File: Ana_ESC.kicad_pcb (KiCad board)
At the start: 4 copper layers, 90 x 90 mm, 106 parts, among them IC3 TCAN330DCNT, J1 BM04B-GHS-TBT_LF__SN__N_, J2 Conn_01x04_Pin, J3 USB_C_Receptacle_USB2.0_16P, J4 BM04B-GHS-TBT_LF__SN__N_, J5 Conn_01x02_Socket, Q10 STL90N6F7, Q11 STL90N6F7, Q12 STL90N6F7, Q7 STL90N6F7, Q8 STL90N6F7, Q9 STL90N6F7, SW1 SW_SPDT, SW2 SW_SPDT, U1 DRV8323RSRGZR, U2 STM32G431CBU6, U3 ME6211C33M5, Y1 ECS-80-20-5PX-TR

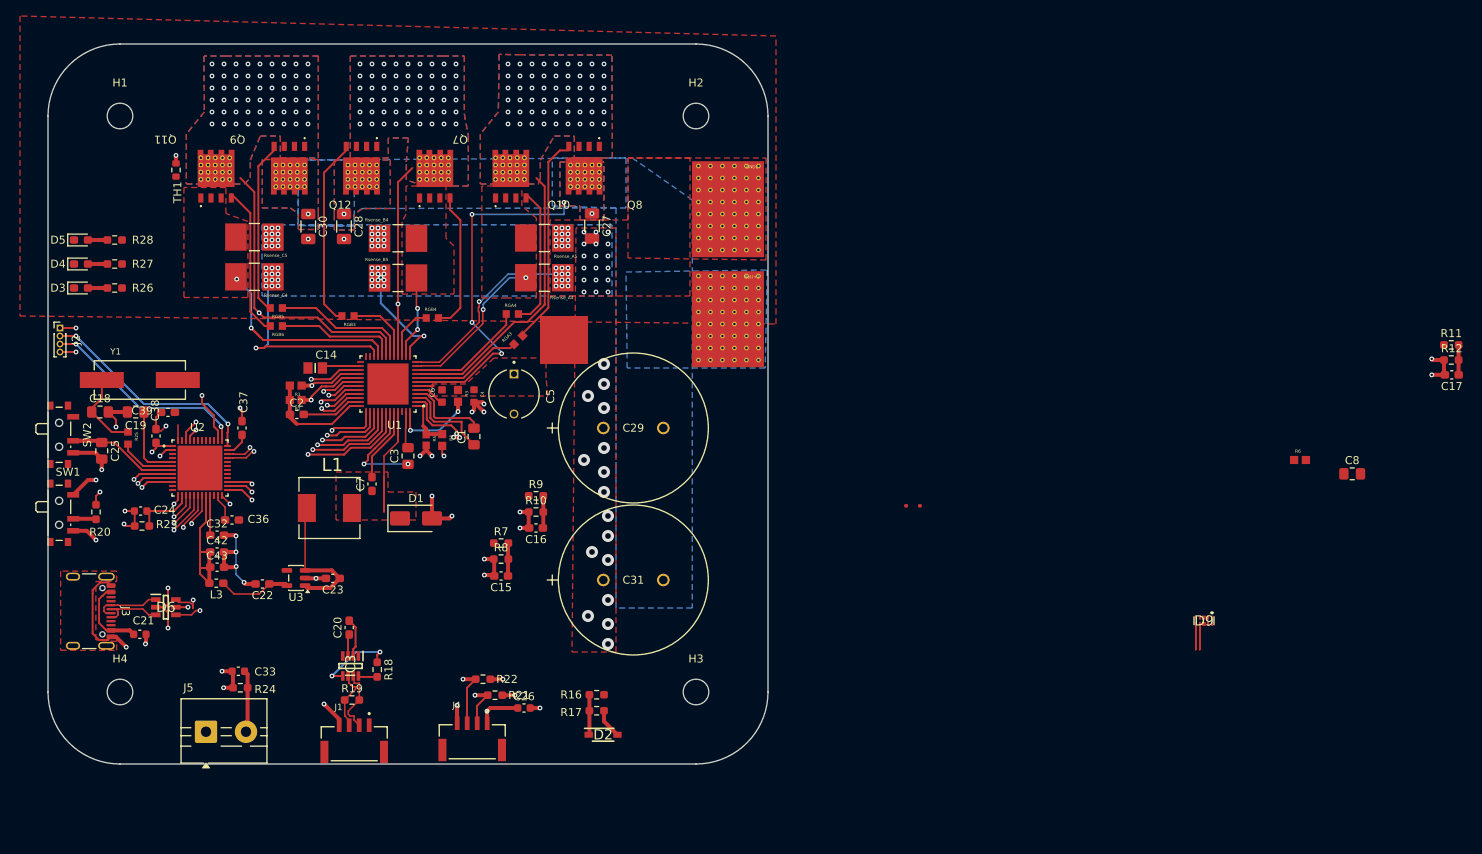
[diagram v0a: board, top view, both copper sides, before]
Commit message: Some pcb design and schematics editings about PGND_DRV
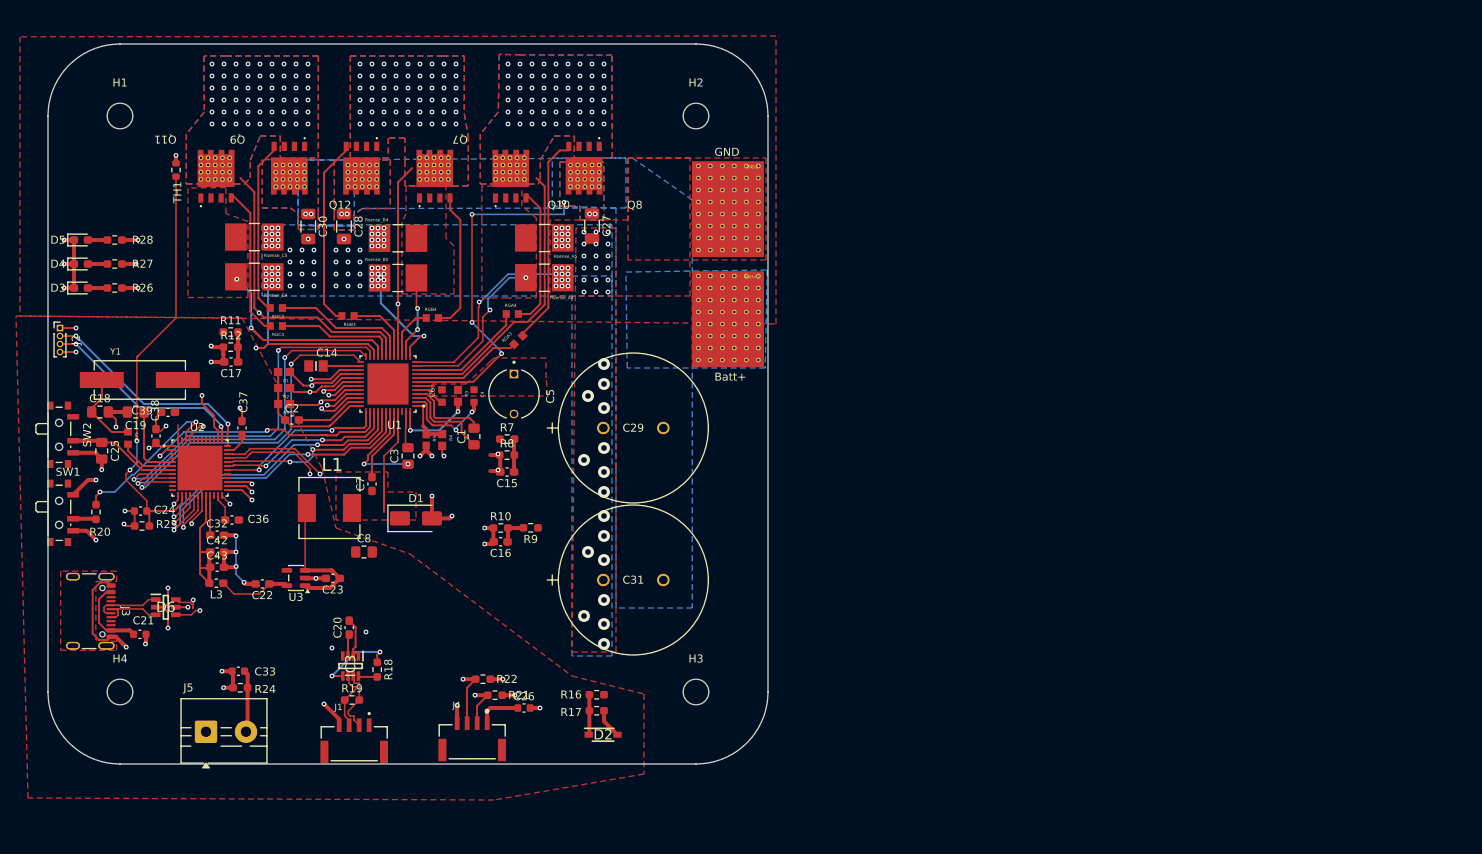
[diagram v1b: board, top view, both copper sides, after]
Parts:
- removed D9: ESD7104MUTAG, LIB_ESD7104MUTAG:ESD8104MUTAG
- removed NT1: NetTie_4, NetTie:NetTie-4_SMD_Pad2.0mm
- moved C17 152.6 mm to (71.4, 91.2)
- moved R11 152.6 mm to (71.3, 87.5)
- moved R12 152.6 mm to (71.3, 89.4)
- moved R6 127.2 mm to (78.0, 96.5), turned to 180 degrees
- moved C8 123.9 mm to (88.0, 115.0)
- moved C15 13.0 mm to (105.9, 105.0)
- moved R7 13.0 mm to (105.9, 100.9)
- moved R8 13.0 mm to (105.9, 102.9)
- moved R10 4.84 mm to (105.1, 112.0)
- moved C16 4.74 mm to (105.1, 113.7)
- moved R9 4.05 mm to (108.8, 112.0), turned to 180 degrees
- moved R1 2.24 mm to (78.0, 92.5)
- moved R2 2.09 mm to (78.0, 94.5)
- moved C2 0.93 mm to (79.0, 98.5)
- moved C14 0.27 mm to (82.0, 91.8)
- renumbered RGB5 to RGC3, RGB6 to RGC4
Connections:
- C27 pad 2: PGND -> PGND_DRV
- C28 pad 2: GND -> PGND_DRV
- C29 pad 1: GND -> PGND_DRV
- C30 pad 2: GND -> PGND_DRV
- C31 pad 1: GND -> PGND_DRV
- C4 pad 2: /Gate_Driver/PGND -> PGND_DRV
- C5 pad N: /Gate_Driver/PGND -> PGND_DRV
- GND1 pad 1: GND -> PGND_DRV
- Rsense_A4 pad 1: PGND -> PGND_DRV
- Rsense_A5 pad 1: PGND -> PGND_DRV
- Rsense_B4 pad 1: GND -> PGND_DRV
- Rsense_B5 pad 1: GND -> PGND_DRV
- Rsense_C4 pad 1: GND -> PGND_DRV
- Rsense_C5 pad 1: GND -> PGND_DRV
- U1 pad 12: PGND -> PGND_DRV
- U1 pad 13: GND -> PGND_DRV
- U1 pad 22: GND -> PGND_DRV
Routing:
- net PGND_DRV: track 0.00 -> 67.3 mm, vias 0 -> 136
- net /MCU/NTC_FET: track 7.89 -> 53.4 mm, vias 0 -> 2
- net /Gate_Driver/SOC: track 5.10 -> 48.0 mm, vias 1 -> 2
- net /Gate_Driver/SOB: track 4.60 -> 45.6 mm, vias 1 -> 2
- net /Gate_Driver/SOA: track 4.10 -> 43.4 mm, vias 1 -> 2
- net GND: track 147.6 -> 115.6 mm, vias 102 -> 35
- net PGND: track 24.9 -> 0.00 mm, vias 42 -> 0
- net /Gate_Driver/INLB: track 16.0 -> 39.6 mm
- net /Gate_Driver/INLA: track 9.62 -> 32.2 mm
- net /Gate_Driver/INLC: track 18.4 -> 39.1 mm
- net /MCU/BOOT0: track 4.63 -> 20.3 mm
- net /Gate_Driver/INHA: track 6.29 -> 21.7 mm, vias 1 -> 2
- net /Gate_Driver/INHB: track 9.17 -> 22.5 mm, vias 1 -> 2
- net /Gate_Driver/INHC: track 12.1 -> 24.0 mm, vias 1 -> 2
- net /MCU/USB_DP: track 9.79 -> 16.4 mm
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- added copper zone on B.Cu, net PGND_DRV
- added copper zone on F.Cu, net PGND_DRV
- removed copper zone on B.Cu, net GND
- removed copper zone on F.Cu, net PGND
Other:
- board text added: "Batt+"
- board text added: "GND"

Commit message: all routed pcb
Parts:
- moved D3 61.9 mm to (98.3, 123.8), turned to 180 degrees
- moved D4 61.9 mm to (98.3, 120.8), turned to 180 degrees
- moved D5 61.9 mm to (98.3, 117.8), turned to 180 degrees
- moved R26 56.0 mm to (94.1, 123.8), turned to 180 degrees
- moved R27 56.0 mm to (94.1, 120.8), turned to 180 degrees
- moved R28 56.0 mm to (94.1, 117.8), turned to 180 degrees
- moved C16 28.7 mm to (97.8, 86.0)
- moved R10 25.3 mm to (97.8, 87.8)
- moved R9 25.1 mm to (97.8, 89.5), turned to 0 degrees
- moved J3 23.7 mm to (70.7, 137.9), turned to 0 degrees
- moved R11 23.5 mm to (76.0, 110.5), turned to 180 degrees
- moved C17 23.5 mm to (76.0, 114.2), turned to 0 degrees
- moved R12 23.4 mm to (76.0, 112.4), turned to 180 degrees
- moved J5 22.8 mm to (53.0, 120.5), turned to -90 degrees
- moved R24 15.8 mm to (58.5, 124.8), turned to 90 degrees
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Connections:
- C14 pad 1: /Gate_Driver/DGND -> GND
- C2 pad 2: /Gate_Driver/AGND -> GND
- C3 pad 1: /Gate_Driver/BGND -> GND
- J4 pad 3: /MCU/I2C1_SCL -> /MCU/I2C1_SDA
- R22 pad 2: /MCU/I2C1_SCL -> /MCU/I2C1_SDA
- U1 pad 2: /Gate_Driver/PGND -> GND
- U1 pad 27: /Gate_Driver/DGND -> GND
- U1 pad 35: /Gate_Driver/AGND -> GND
- U1 pad 43: /Gate_Driver/BGND -> GND
- U2 pad 45: /MCU/I2C1_SCL -> /MCU/I2C1_SDA
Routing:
- net /MCU/UART_P: track 0.00 -> 85.0 mm, vias 0 -> 2
- net GND: track 115.6 -> 198.1 mm, vias 35 -> 39
- net /MCU/UART_N: track 0.00 -> 78.8 mm, vias 0 -> 2
- net /MCU/I2C1_SDA: track 0.00 -> 76.0 mm, vias 0 -> 2
- net /MCU/VBus: track 9.21 -> 73.9 mm, vias 1 -> 0
- net +3.3V: track 44.4 -> 102.3 mm, vias 7 -> 15
- net MCU_PWR: track 30.2 -> 85.9 mm, vias 2 -> 4
- net /MCU/I2C1_SCL: track 22.8 -> 74.5 mm, vias 4 -> 2
- net VM: track 51.3 -> 90.2 mm
- net /Gate_Driver/SHC: track 37.3 -> 72.1 mm, vias 55 -> 57
- net Net-(U2-PB12): track 5.58 -> 30.7 mm
- net Net-(U2-PB13): track 5.13 -> 30.1 mm
- net /MCU/USB_DP: track 16.4 -> 41.1 mm
- net /MCU/USB_DN: track 16.0 -> 40.0 mm
- net Net-(U2-PB14): track 5.17 -> 28.5 mm
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- added copper zone on In1.Cu, net +3.3V

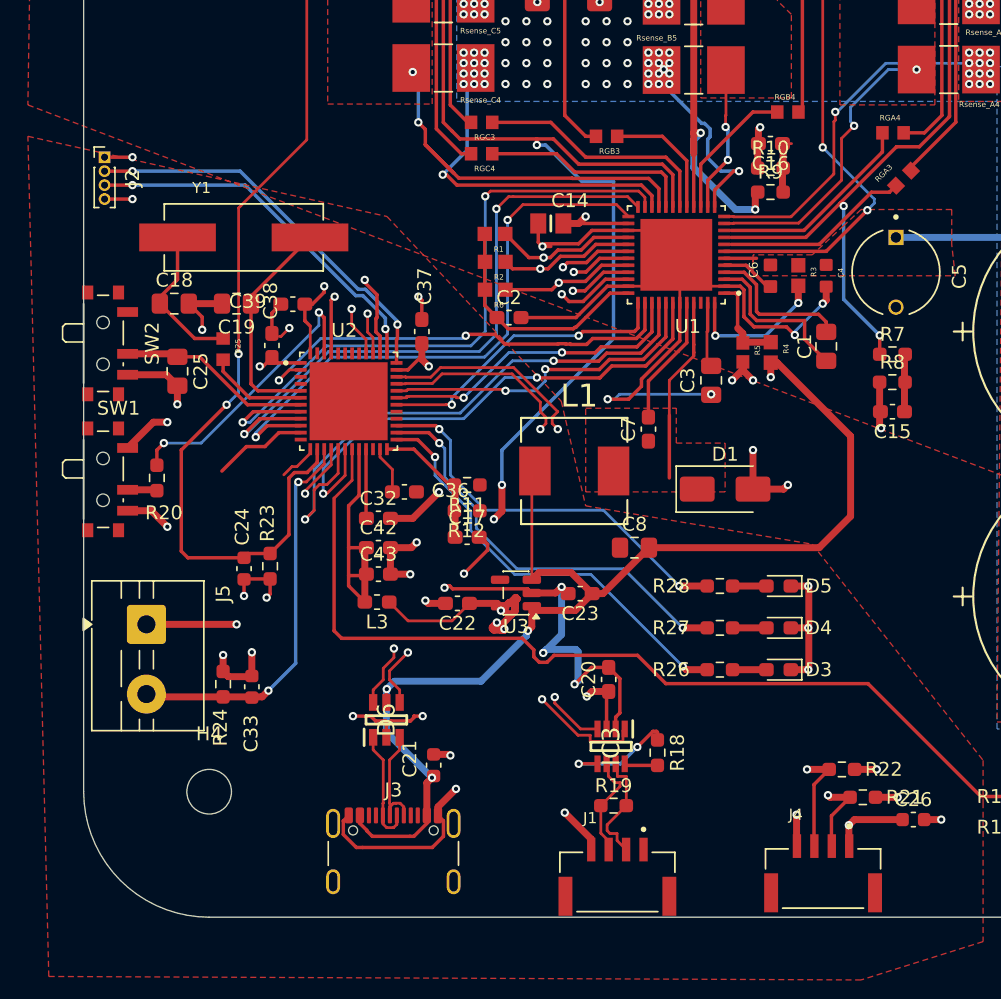
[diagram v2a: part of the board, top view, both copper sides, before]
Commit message: fixing design errors
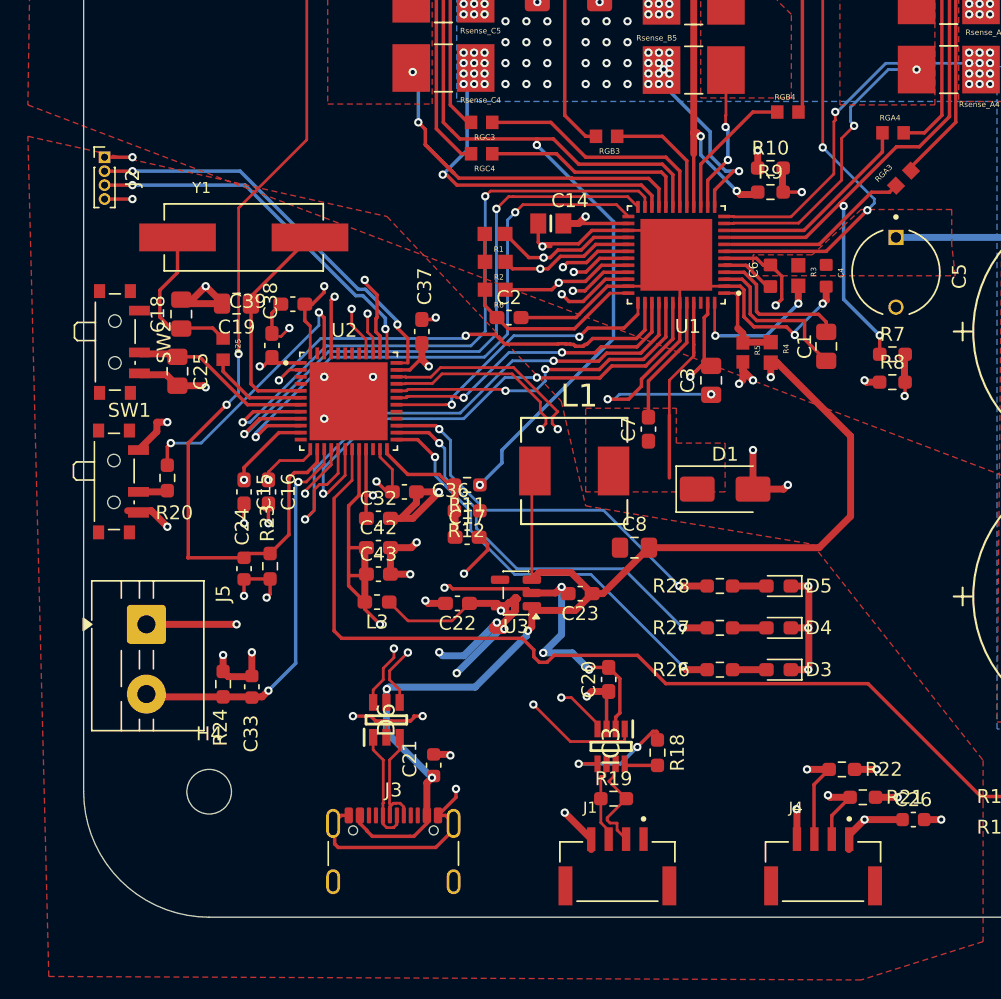
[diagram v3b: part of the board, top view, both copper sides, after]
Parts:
- moved C15 46.9 mm to (60.0, 111.0), turned to -90 degrees
- moved C16 43.8 mm to (61.8, 111.0), turned to -90 degrees
- moved C18 0.90 mm to (55.5, 98.2), turned to 90 degrees
- moved SW2 0.86 mm to (51.1, 100.2)
- moved SW1 0.79 mm to (51.0, 110.2)
- moved J1 0.75 mm to (86.8, 139.2)
- moved R20 0.75 mm to (54.5, 110.0)
- moved J4 0.50 mm to (101.5, 139.2)
- moved R19 0.50 mm to (86.5, 133.0)
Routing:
- net /Gate_Driver/SENS1: track 11.2 -> 92.4 mm, vias 0 -> 2
- net /Gate_Driver/SENS2: track 7.11 -> 61.4 mm, vias 0 -> 2
- net +3.3V: track 102.3 -> 123.5 mm, vias 15 -> 18
- net GND: track 198.1 -> 217.2 mm, vias 39 -> 44
- net VM: track 90.2 -> 106.6 mm, vias 10 -> 12
- net +3.3VA: track 23.2 -> 35.3 mm, vias 0 -> 2
- net /Gate_Driver/SHC: track 72.1 -> 68.4 mm, vias 57 -> 56
- net /Gate_Driver/SHB: track 34.5 -> 31.6 mm
- net /MCU/SWDIO: track 28.5 -> 29.6 mm
- net /MCU/UART_N: track 78.8 -> 79.9 mm
- net /MCU/RST: track 13.6 -> 12.8 mm
- net /MCU/I2C1_SCL: track 74.5 -> 73.8 mm
- net /MCU/I2C1_SDA: track 76.0 -> 75.3 mm
- net /MCU/UART_P: track 85.0 -> 84.3 mm
- net /MCU/BOOT0: track 20.4 -> 19.8 mm
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- added copper zone on In2.Cu, net GND

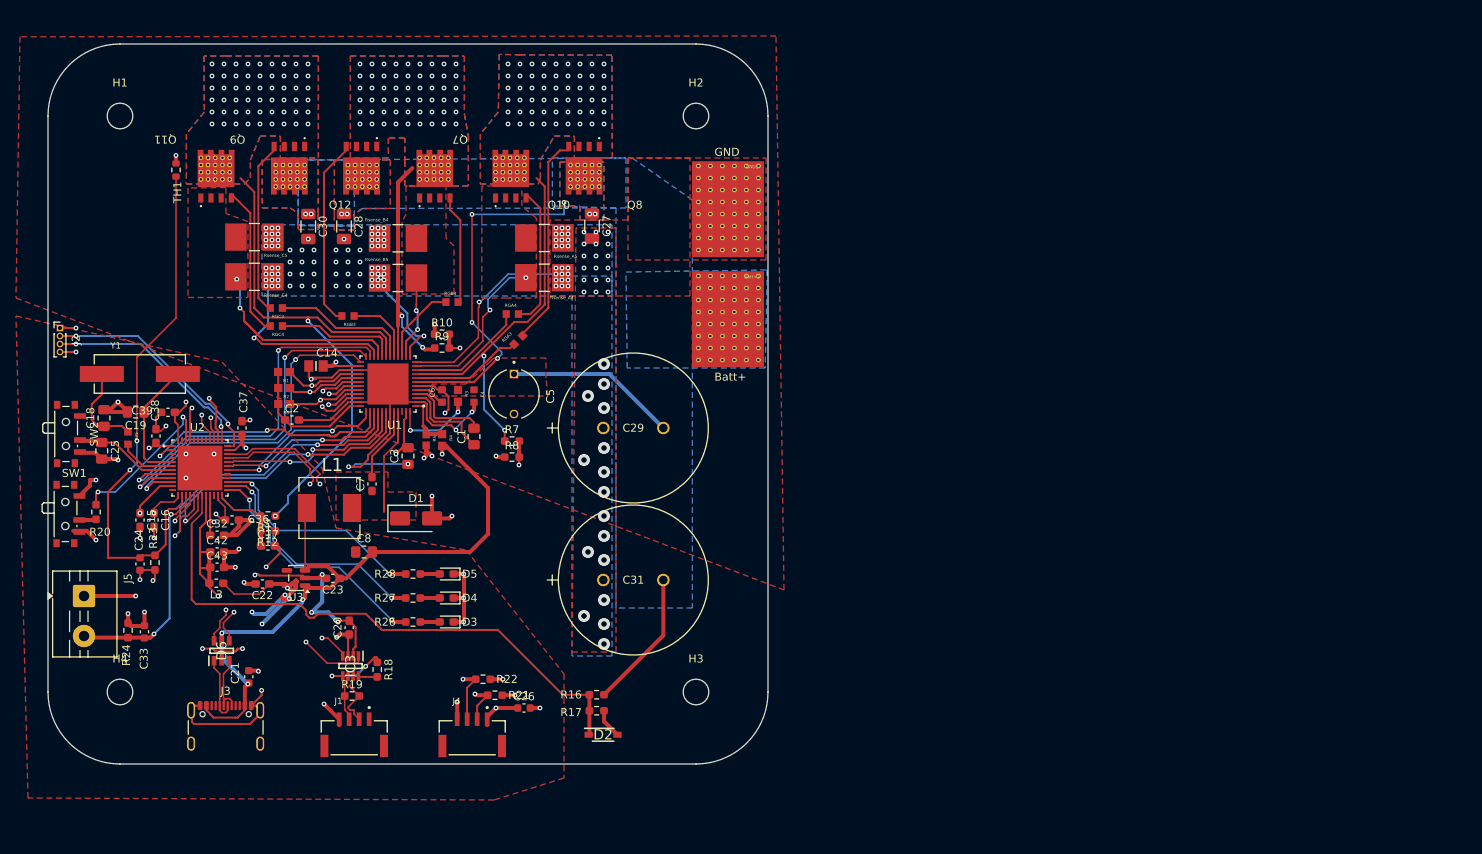
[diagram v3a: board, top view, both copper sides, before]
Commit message: fixing design errors
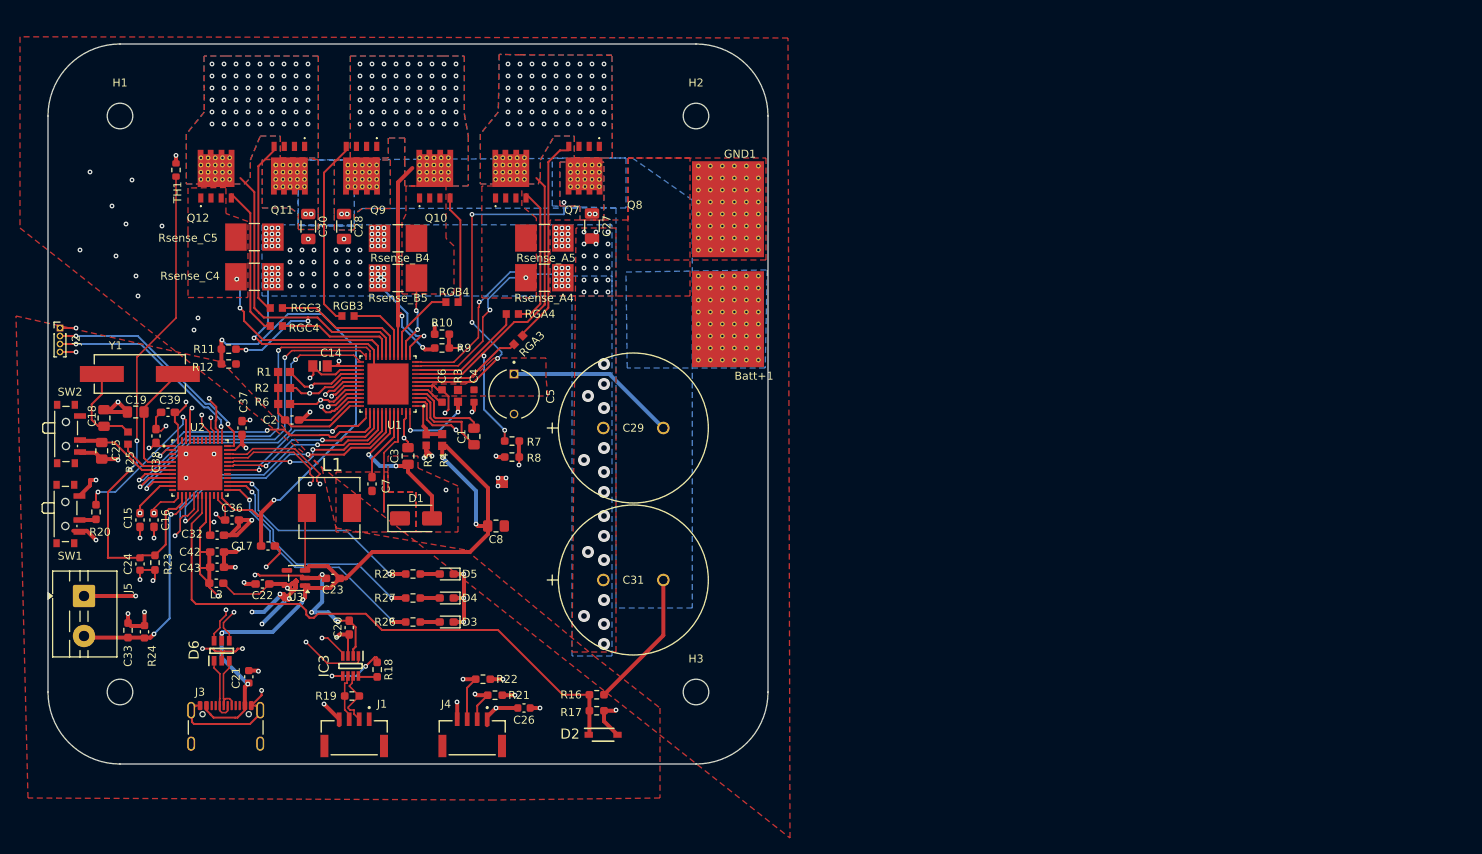
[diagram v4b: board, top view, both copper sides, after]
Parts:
- added NT2: NetTie_4, NetTie:NetTie-4_SMD_Pad0.5mm, F.Cu at (105.2, 106.2)
- moved R11 21.4 mm to (71.1, 89.6)
- moved R12 21.4 mm to (71.1, 91.5)
- moved C8 16.8 mm to (104.5, 111.8), turned to 180 degrees
- moved C14 0.50 mm to (82.5, 91.8)
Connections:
- C14 pad 1: GND -> /Gate_Driver/AGND
- C2 pad 2: GND -> /Gate_Driver/AGND
- C3 pad 1: GND -> /Gate_Driver/BGND
- C8 pad 1: GND -> PGND_DRV
- D1 pad 2: GND -> /Gate_Driver/BGND
- R10 pad 1: GND -> PGND_DRV
- R12 pad 1: GND -> PGND_DRV
- R5 pad 2: GND -> /Gate_Driver/AGND
- R8 pad 1: GND -> PGND_DRV
- U1 pad 2: GND -> /Gate_Driver/PGND
- U1 pad 27: GND -> /Gate_Driver/AGND
- U1 pad 35: GND -> /Gate_Driver/AGND
- U1 pad 43: GND -> /Gate_Driver/BGND
- U1 pad 49: GND -> PGND_DRV
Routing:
- net GND: track 217.2 -> 145.5 mm, vias 44 -> 35
- net /Gate_Driver/AGND: track 0.00 -> 61.9 mm, vias 0 -> 5
- net /Gate_Driver/SENS3: track 9.84 -> 59.8 mm, vias 0 -> 2
- net /Gate_Driver/BGND: track 0.00 -> 26.8 mm, vias 0 -> 4
- net /Gate_Driver/SHC: track 68.4 -> 48.3 mm
- net /Gate_Driver/PGND: track 0.00 -> 17.1 mm, vias 0 -> 2
- net MCU_PWR: track 85.9 -> 98.0 mm, vias 4 -> 5
- net PGND_DRV: track 67.1 -> 74.0 mm, vias 137 -> 150
- net VM: track 106.6 -> 102.0 mm
- net unconnected-(U2-PC4-Pad16): track 3.97 -> 0.00 mm, vias 1 -> 0
- net /Gate_Driver/SPC: track 27.8 -> 25.0 mm
- net +3.3V: track 123.5 -> 124.1 mm
- added copper zone on F.Cu, net /Gate_Driver/BGND
- added copper zone on In2.Cu, net PGND_DRV
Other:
- board text removed: "Batt+"
- board text removed: "GND"
